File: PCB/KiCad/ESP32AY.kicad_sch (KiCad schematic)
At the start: 104 parts, among them J1 ZX62D-B-5P8, J2 MiniJack, J3 SD Card, Q1 BC807, Q2 BC817, Q3 BC817, SW1 SW_Push, SW2 EN, SW3 BOOT, U1 AY-3-8910, U2 AY-3-8910, U3 CH340G, U4 ESP32-WROOM-32, U5 TPA6130A2RTJTG4, U6 SM5308, U7 AMS1117-3.3, U8 74HC595, U9 74HC595, Y3 12MHz

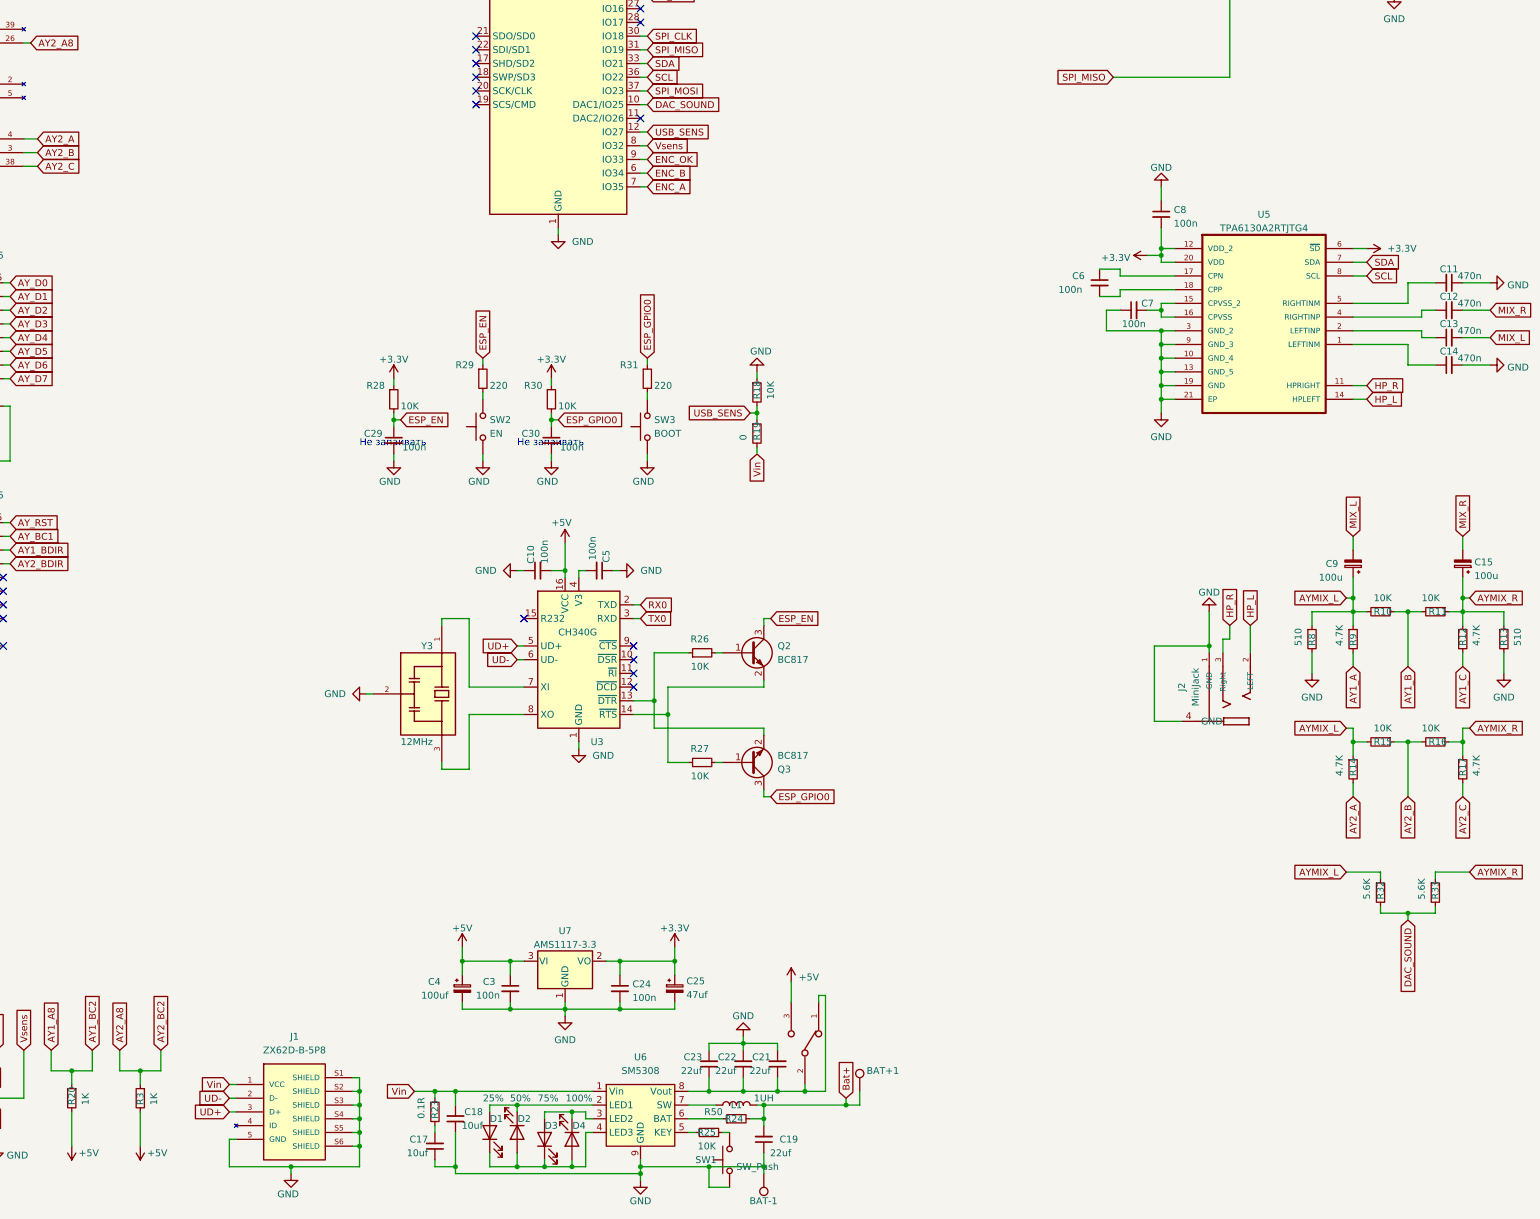
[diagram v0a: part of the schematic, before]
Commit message: PCB Rev. B (Type-C and Stereo DAC)
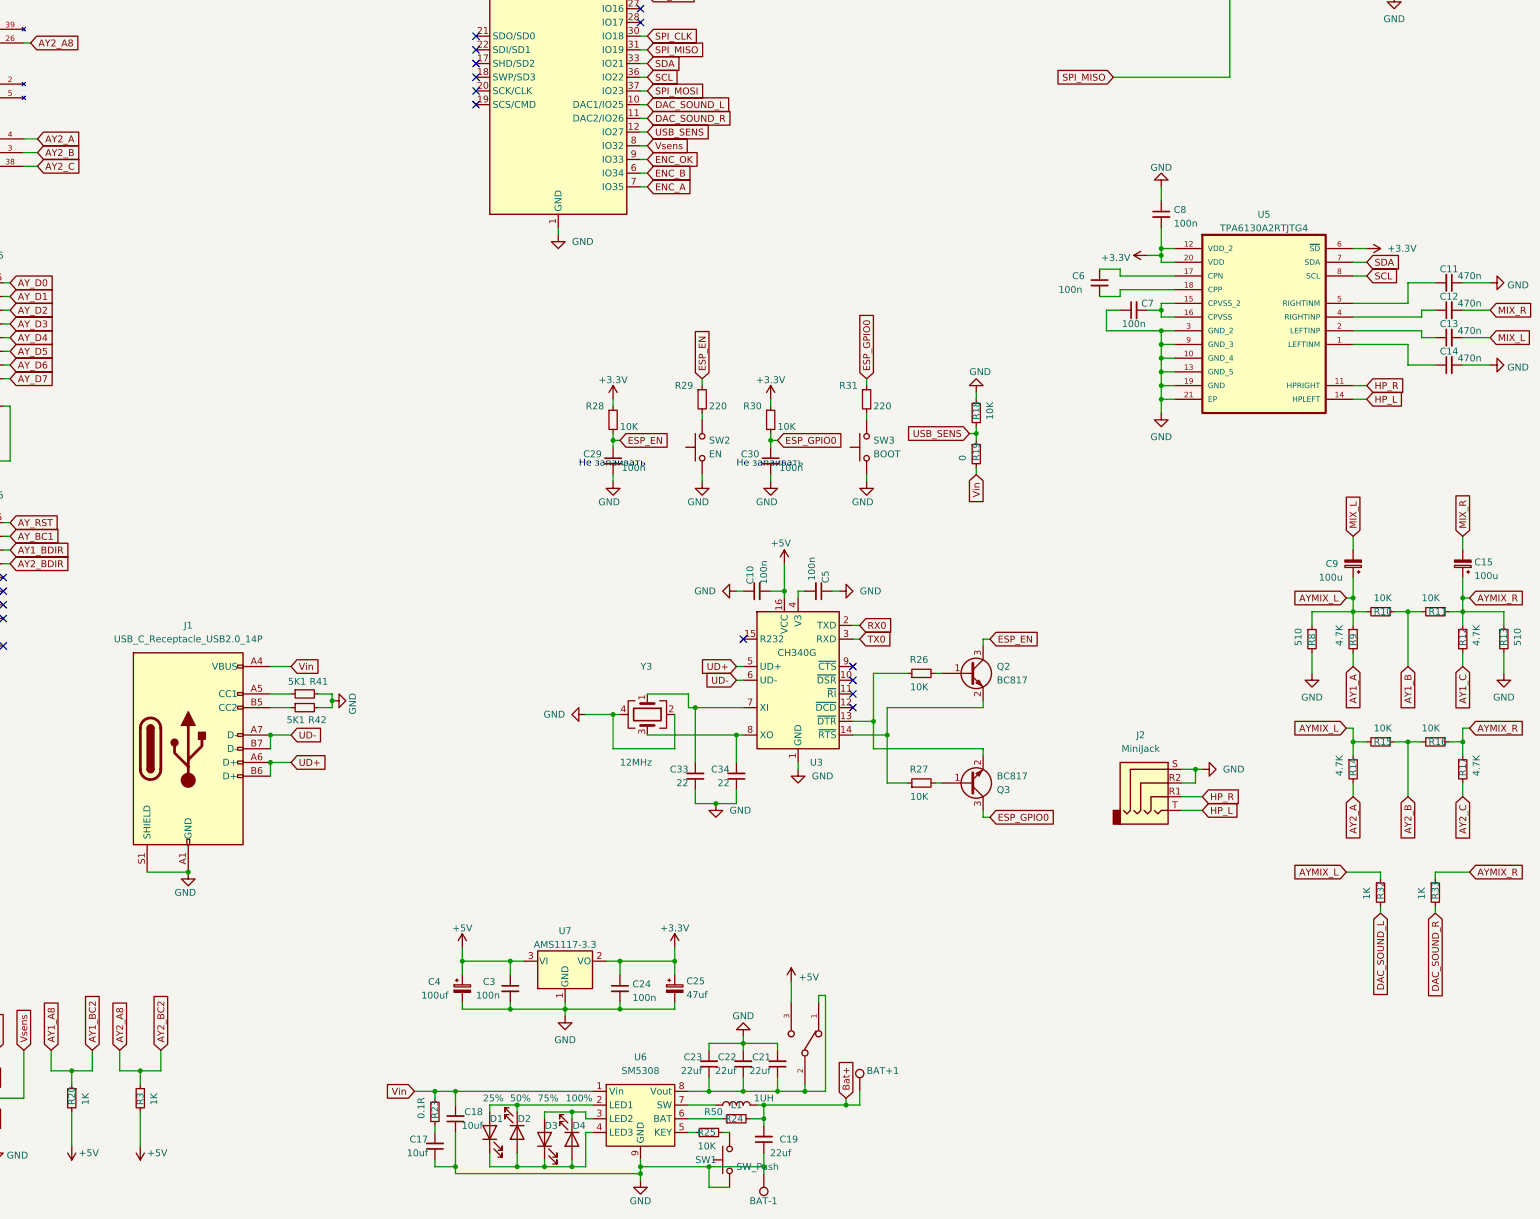
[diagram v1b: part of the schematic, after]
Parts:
- removed J1: ZX62D-B-5P8, mod:HRS_ZX62D-B-5P8, symbol ZX62D-B-5P8:ZX62D-B-5P8
- removed J2: MiniJack, mod:Jack_3.5mm_PJ320D_Horizontal, symbol 35RAPC2BHN2:MiniJack
- added C33, C34: 22, Capacitor_SMD:C_0805_2012Metric_Pad1.18x1.45mm_HandSolder, symbol Device:C_Small
- added J1: USB_C_Receptacle_USB2.0_14P, Connector_USB:USB_C_Receptacle_G-Switch_GT-USB-7010ASV, symbol Connector:USB_C_Receptacle_USB2.0_14P
- added J2: MiniJack, footprints:AUDIO_JACK_3.5MM_SMD_TRRS_rounded_mixed, symbol Connector_Audio:AudioJack4
- added R41, R42: 5K1, Resistor_SMD:R_0805_2012Metric_Pad1.20x1.40mm_HandSolder, symbol Device:R_Small
- C1, C10, C11, C12, C13, C14, C16, C17, C18, C19, C2, C20, C21, C22, C24, C26, C27, C28, C29, C3, C30, C31, C32, C5, C6, C7, C8: footprint Capacitor_SMD:C_1206_3216Metric -> Capacitor_SMD:C_0805_2012Metric_Pad1.18x1.45mm_HandSolder
- C15, C9: footprint Capacitor_Tantalum_SMD:CP_EIA-7360-38_Kemet-E -> Capacitor_Tantalum_SMD:CP_EIA-7343-31_Kemet-D_Pad2.25x2.55mm_HandSolder
- C25, C4: footprint Capacitor_Tantalum_SMD:CP_EIA-7360-38_Kemet-E -> footprints:CP_EIA-7343-31_Kemet-D-uni
- R1, R10, R11, R12, R13, R14, R15, R16, R17, R18, R19, R2, R20, R21, R22, R26, R27, R28, R29, R3, R30, R31, R34, R35, R36, R37, R38, R39, R4, R40, R5, R6, R7, R8, R9: footprint Resistor_SMD:R_1206_3216Metric -> Resistor_SMD:R_0805_2012Metric_Pad1.20x1.40mm_HandSolder
- R32, R33: value 5.6K -> 1K; footprint Resistor_SMD:R_1206_3216Metric -> Resistor_SMD:R_0805_2012Metric_Pad1.20x1.40mm_HandSolder
- SW2, SW3: footprint Button_Switch_SMD:SW_SPST_B3U-1000P -> footprints:SW_SPST_PTS810_handsoldering
- Y3: footprint mod:OSC_CSTCE16M0V53-R0 -> Crystal:Crystal_SMD_3225-4Pin_3.2x2.5mm_HandSoldering; symbol CSTCE16M:CSTCE16M0V53-R0 -> Device:Crystal_GND24
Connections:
- net GND: now also Y3.4, C33.1, C34.1, J1.A1 (GND), J1.A12 (GND), J1.B1 (GND), J1.B12 (GND), J1.S1 (SHIELD), J2.R2, J2.S, R41.2, R42.2
- net HP_L: now also J2.T
- net HP_R: now also J2.R1
- net UD+: now also J1.A6 (D+), J1.B6 (D+)
- net UD-: now also J1.A7 (D-), J1.B7 (D-)
- net Vin: now also J1.A4 (VBUS), J1.A9 (VBUS), J1.B4 (VBUS), J1.B9 (VBUS)
- net DAC_SOUND_R: now reaches U4.11 (DAC2/IO26)
- net DAC_SOUND_R: now also R33.2
- net at U3.7 (XI), Y3.1: now also C33.2
- net at U3.8 (XO), Y3.3: now also C34.2
- net DAC_SOUND renamed DAC_SOUND_L
- net DAC_SOUND_L: no longer R33.2
- new net: J1.A5 (CC1), R41.1
- new net: J1.B5 (CC2), R42.1
- no-connect marks 57 -> 56
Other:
- title: ESP32 AY Player -> ESP32 AY Player Rev.B
- moved on the sheet: C10, C29, C30, C5, Q2, Q3, R18, R19, R26, R27, R28, R29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

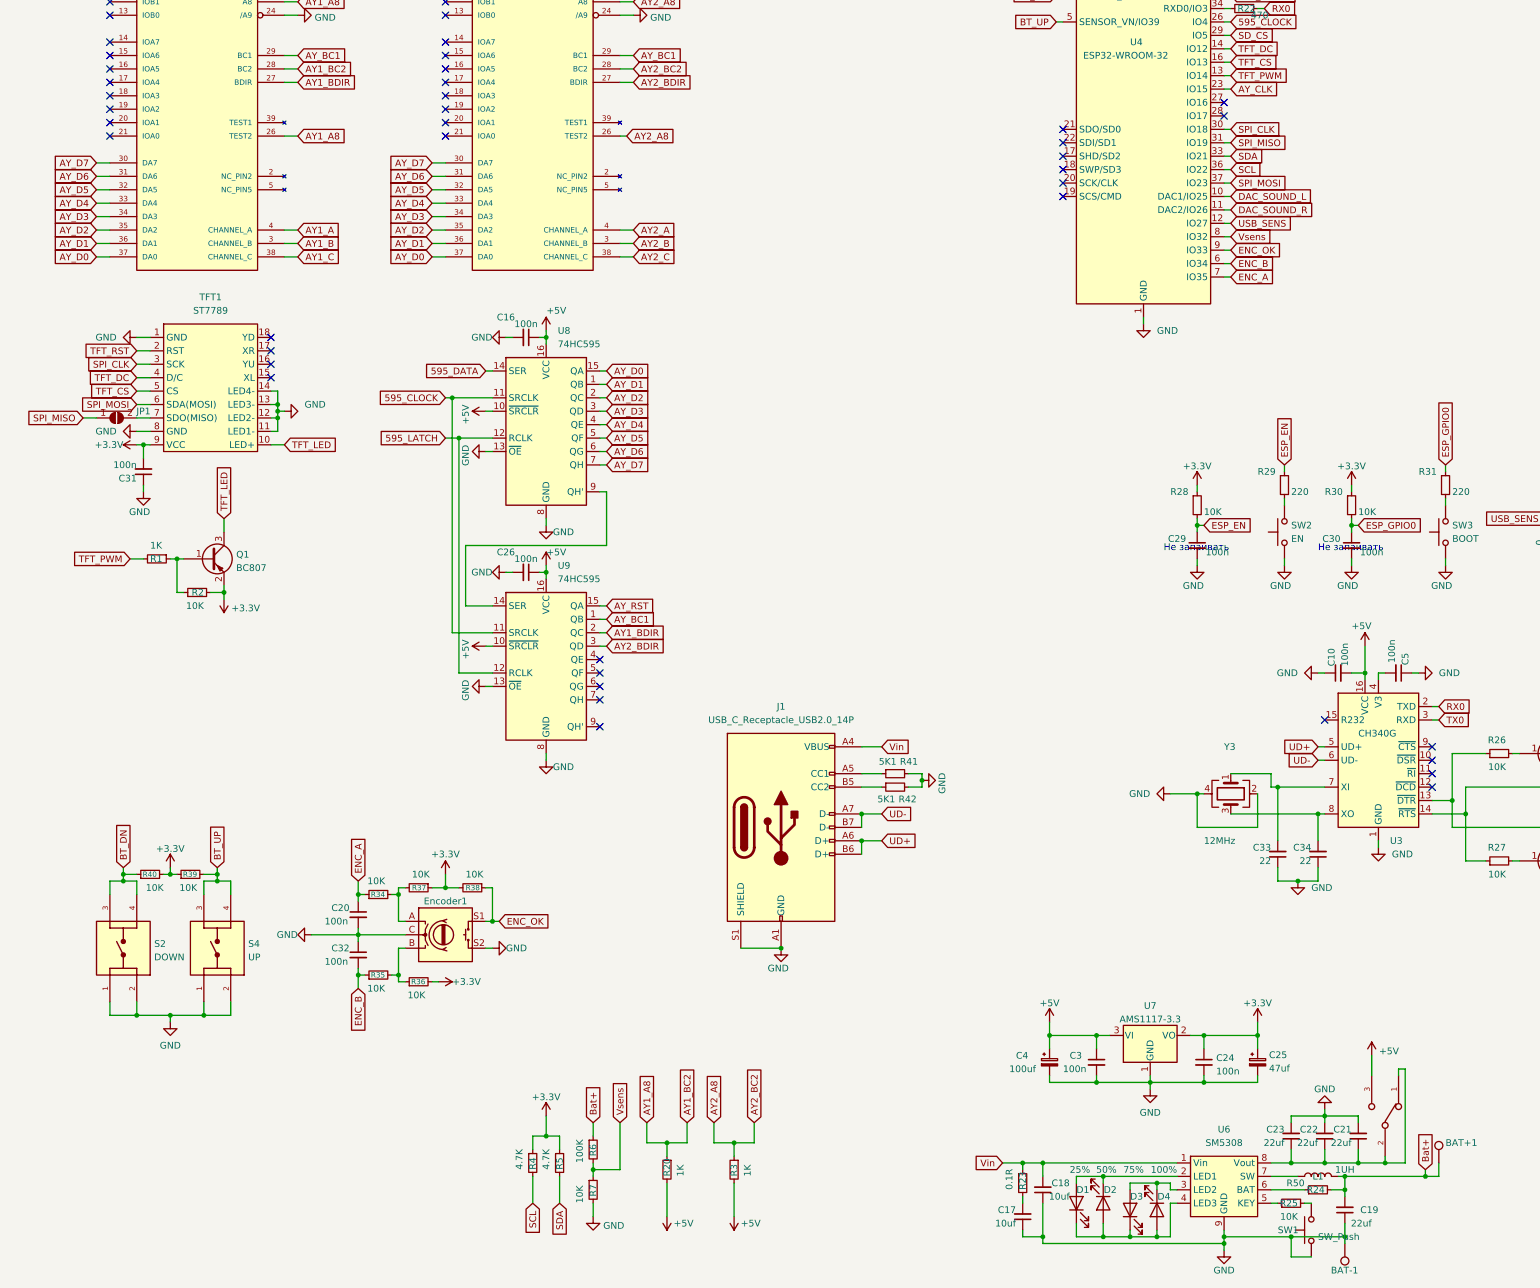
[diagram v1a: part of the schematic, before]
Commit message: Release 3.4 (added mod+s3m formats), LCD moved to dedicated SPI with revision C PCB or soldering upgrade from revision A and B to revision C (see README). Some optimizations and new features.
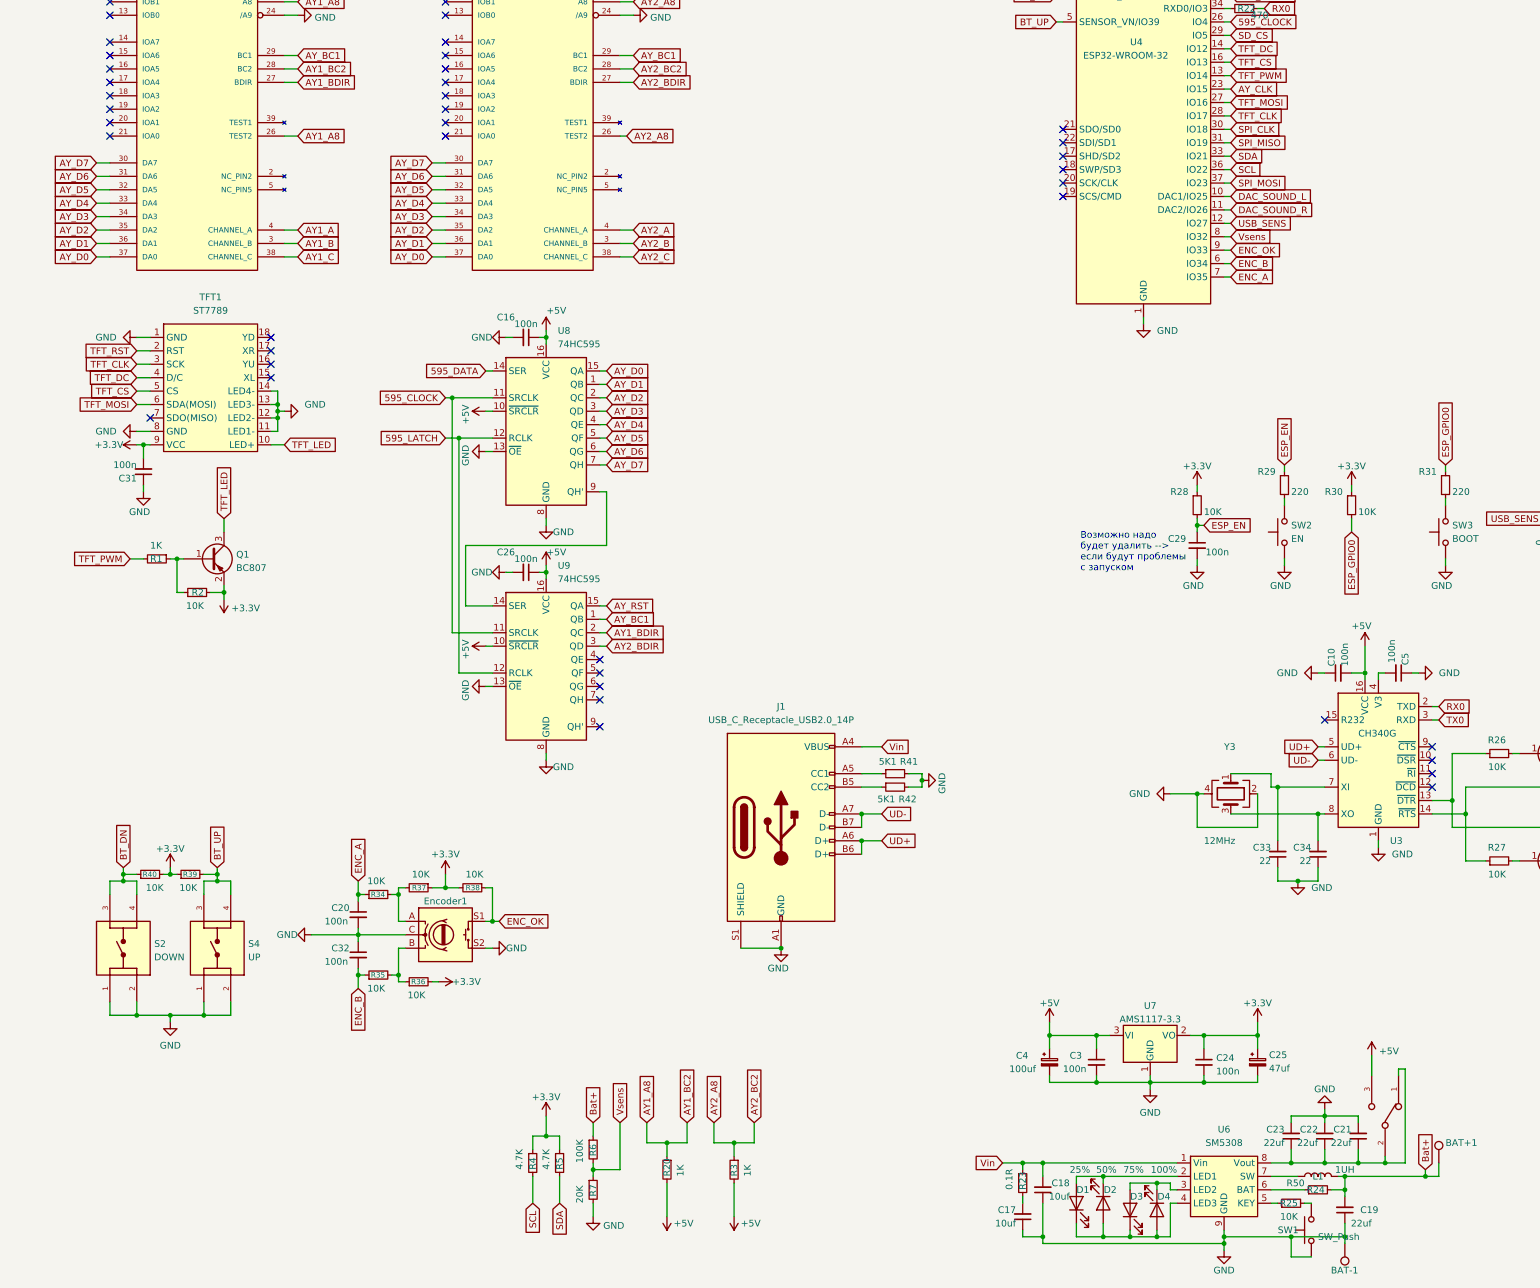
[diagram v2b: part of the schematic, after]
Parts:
- removed C30: 100n, Capacitor_SMD:C_0805_2012Metric_Pad1.18x1.45mm_HandSolder, symbol Device:C_Small
- removed JP1: jumper, Jumper:SolderJumper-2_P1.3mm_Bridged_RoundedPad1.0x1.5mm, symbol Jumper:SolderJumper_2_Open
- R7: value 10K -> 20K
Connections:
- net SPI_CLK: no longer TFT1.3 (SCK)
- net SPI_MOSI: no longer TFT1.6 (SDA(MOSI))
- net TFT_MOSI: now reaches U4.27 (IO16)
- net TFT_MOSI: now also TFT1.6 (SDA(MOSI))
- net TFT_CLK: now reaches U4.28 (IO17)
- net TFT_CLK: now also TFT1.3 (SCK)
- no-connect marks 56 -> 55
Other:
- note added: "Возможно надо будет удалить --> если будут проблемы с запуском"
- note removed: "Не запаивать"
- title: ESP32 AY Player Rev.B -> ZxPod Player Rev.C

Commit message: Refactored schematics, updated BOM
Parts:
- C33, C34: value 22 -> 22p
- R24: value R50 -> 0.5R
- R29, R31, SW2, SW3: now not fitted; now left out of the parts list
- SW1: value SW_Push -> Check bat
- U6: value SM5308 -> IP5306
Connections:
- net +3.3V: now also C28.2; no longer C28.1
- net GND: now also C28.1; no longer C28.2
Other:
- note added: "3.3v LDO"
- note added: "Audio AMP"
- note added: "Audio Mixer"
- note added: "Battery & USB sense"
- note added: "Controls"
- note added: "ESP32 Module"
- note added: "Please make sure to use exactly the same IP5306 IC. Other ICs (like FM5324, SM5308) has some issues with sleep/wakeup modes."
- note added: "SD card"
- note added: "TFT Display and brightness control"
- note added: "Turbosound"
- note added: "USB Charger and step-up SoC"
- note added: "USB UART"
- note removed: "Возможно надо будет удалить --> если будут проблемы с запуском"
- moved on the sheet: BAT+1, BAT-1, C1, C10, C11, C12, C13, C14, C15, C16, C17, C18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

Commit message: Updated page settings (revision number, etc)
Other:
- title: ZxPod Player Rev.C -> ZxPod Player
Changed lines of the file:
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@@
 	(paper "A3")
 	(title_block
-		(title "ZxPod Player Rev.C")
-		(date "2025-03-03")
+		(title "ZxPod Player")
+		(date "2025-04-10")
+		(rev "C")
 		(company "Spawn")
 		(comment 2 "Spawn")
